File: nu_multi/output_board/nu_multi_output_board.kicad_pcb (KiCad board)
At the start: 2 copper layers, 40 x 18.2 mm, 3 parts, among them J1 CONN_02X07, J2 CONN_02X05

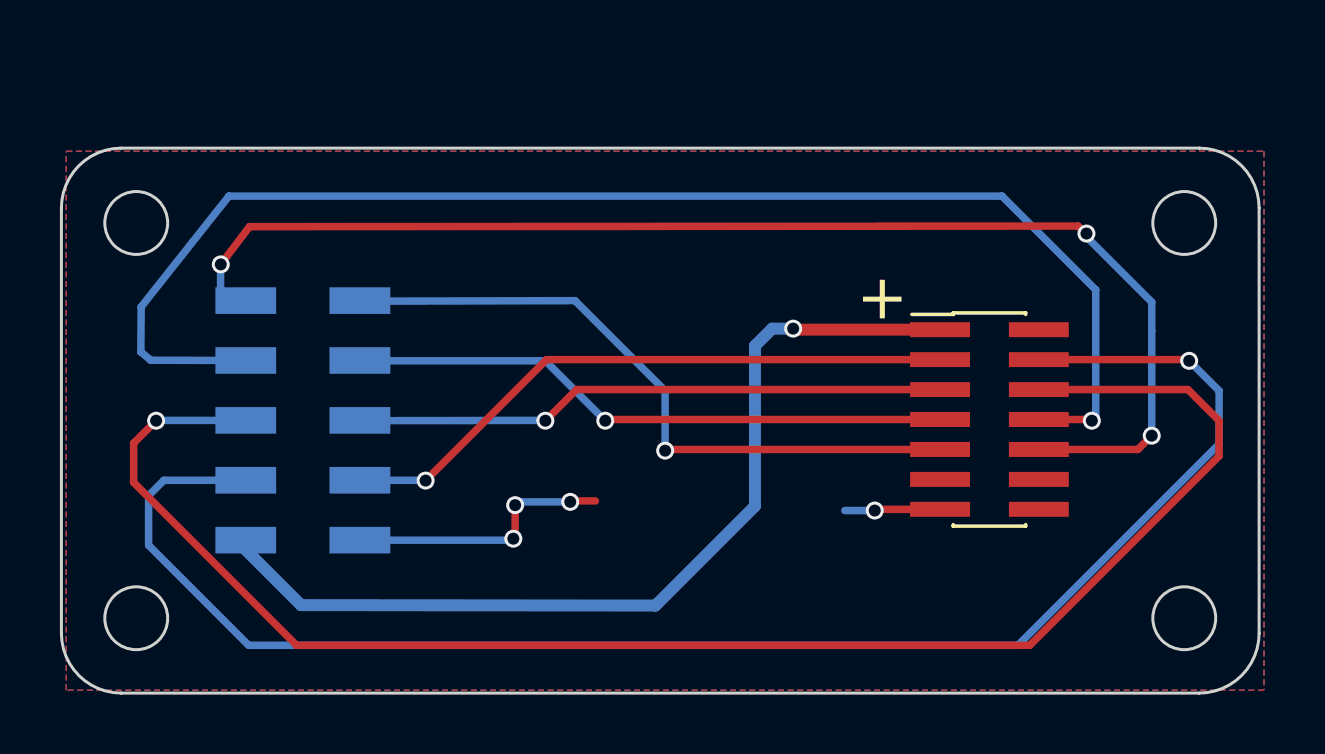
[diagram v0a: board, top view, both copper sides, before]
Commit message: strict 1mm grid; re-layout
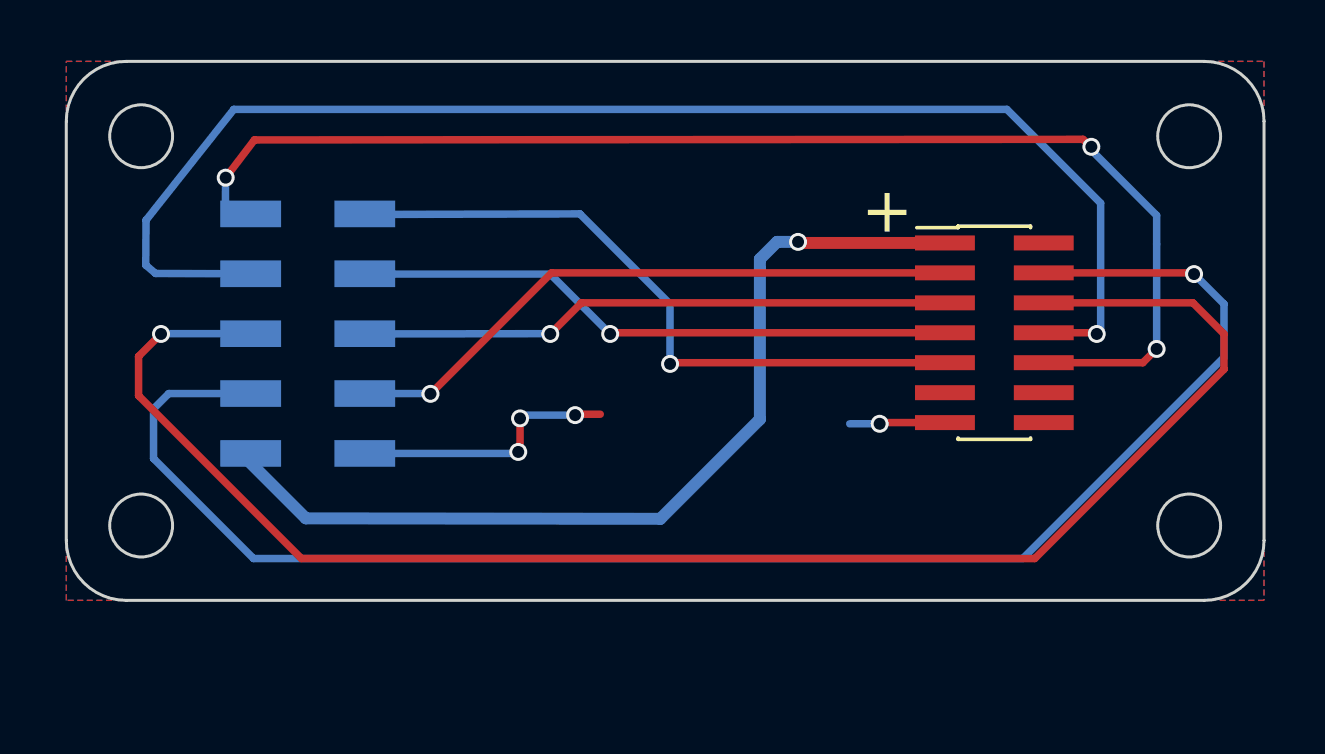
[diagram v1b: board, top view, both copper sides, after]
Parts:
- removed the G*** at (148.2, 69.2)
- added G***: LOGO, cycfi_library:cycfi-logo-15mm, B.Cu at (148.8, 66.5)
- moved J1 2.90 mm to (153.0, 59.1)
- moved J2 2.90 mm to (130.1, 59.1)
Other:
- board size 40 x 18.2 mm -> 40 x 18 mm

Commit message: Updated output board
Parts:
- J1: value CONN_02X07 -> Conn_02x07_Odd_Even
- J2: value CONN_02X05 -> Conn_02x05_Odd_Even
- moved G*** 1.36 mm to (148.6, 65.1)
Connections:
- net Net-(J1-Pad1) renamed V+
- net Net-(J1-Pad10) renamed CH7
- net Net-(J1-Pad3) renamed CH2
- net Net-(J1-Pad4) renamed CH1
- net Net-(J1-Pad5) renamed CH4
- net Net-(J1-Pad6) renamed CH3
- net Net-(J1-Pad7) renamed CH6
- net Net-(J1-Pad8) renamed CH5
- net Net-(J1-Pad9) renamed CH8
- J1 pad 11: GND -> CH10
- J1 pad 12: GND -> CH9
- J1 pad 13: GND -> CH12
- J1 pad 14: GND -> CH11
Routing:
- net GND: track 12.2 -> 8.22 mm, vias 4 -> 3
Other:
- net class Default removed
- board text added: "Output Board 2.5.1"

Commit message: Updated. Use cycfi library.
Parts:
- J1: footprint Pin_Headers:Pin_Header_Straight_2x07_Pitch1.00mm_SMD -> cycfi_library:pin_header_2x7p_1.00mm_smd_vertical
- J2: footprint Cycfi_Kicad_Headers:2x5_1mm_Angled_SMD -> cycfi_library:2x5_2mm_Nu_Multi_SMD
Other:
- board text added: "Output Board 2.5.2"
- board text removed: "Output Board 2.5.1"
